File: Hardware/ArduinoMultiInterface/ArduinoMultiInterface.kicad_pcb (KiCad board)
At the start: 2 copper layers, 119.9 x 64.3 mm, 28 parts, among them J1 PORT1, J2 I2C, J3 SPI, J4 SER, SW1 SW_RESET, U1 ATmega328-P, U2 74HC165, U3 74HC595, U4 74HC574, U5 74HC574, U6 74HC574, U7 74HC04, U9 74LS20, Y1 20MHz

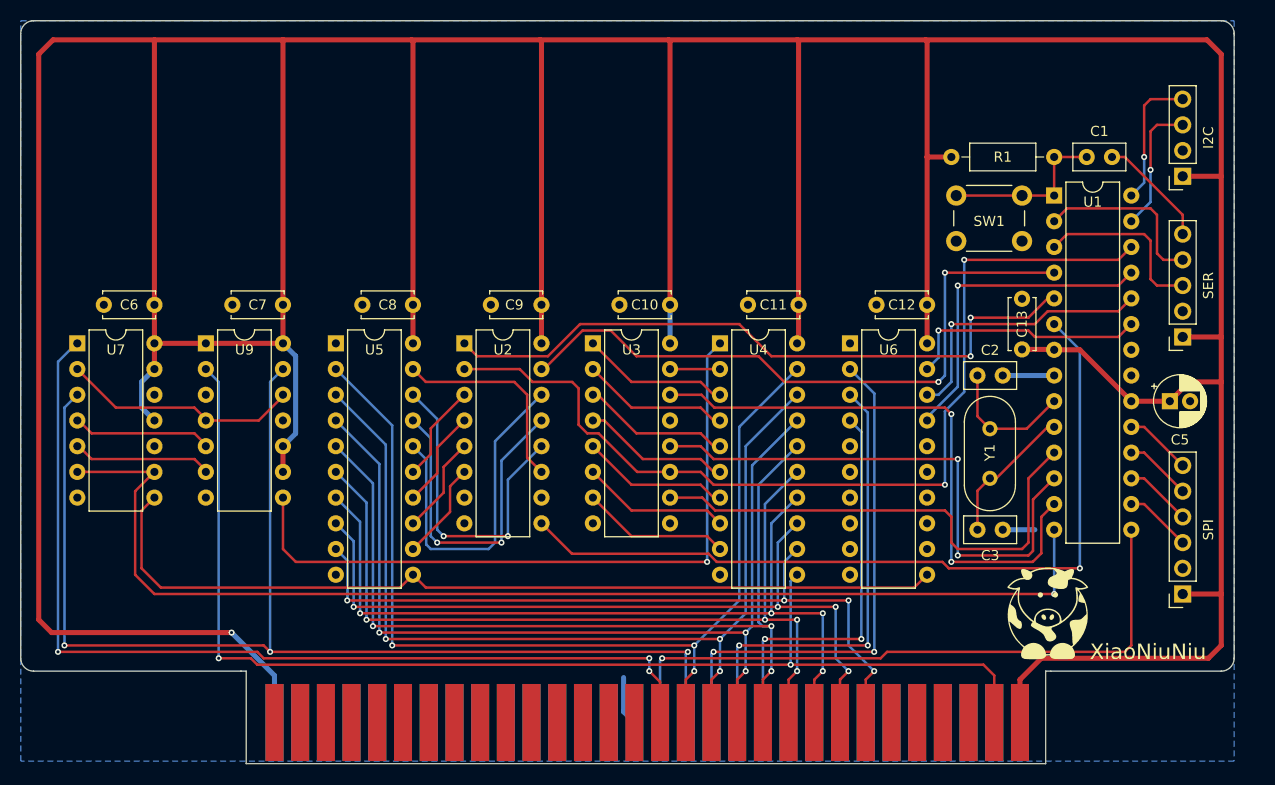
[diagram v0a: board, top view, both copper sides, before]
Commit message: Add nfr24l01 protocol
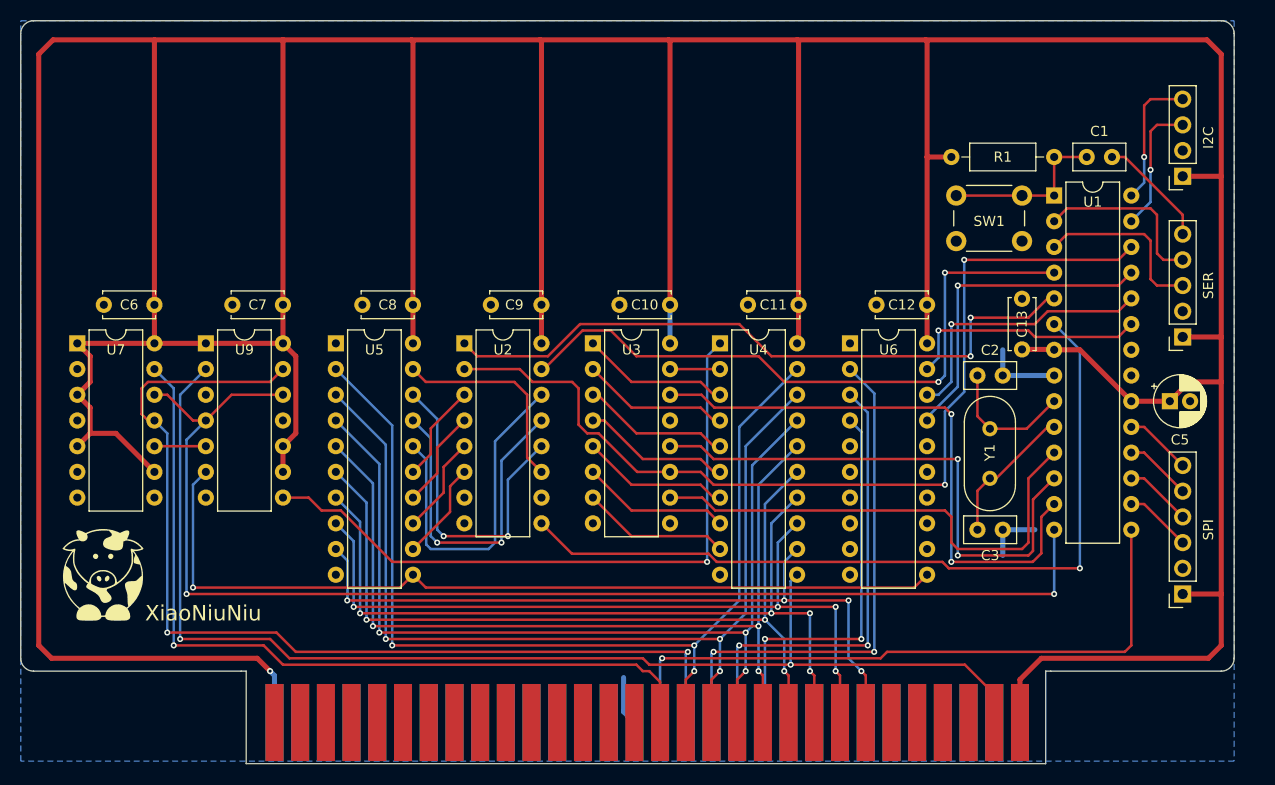
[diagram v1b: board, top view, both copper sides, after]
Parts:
- moved XiaoNiuNiu 93.4 mm to (97.8, 130.2)
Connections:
- U7 pad 1: /PORT1CSB -> +5V
- U7 pad 10: unconnected-(U7-Pad10) -> Net-(U7-Pad10)
- U7 pad 11: +5V -> /RW
- U7 pad 12: unconnected-(U7-Pad12) -> PCINT
- U7 pad 13: +5V -> /PORT1CSB
- U7 pad 2: Net-(U7-Pad2) -> unconnected-(U7-Pad2)
- U7 pad 3: /RW -> +5V
- U7 pad 4: Net-(U7-Pad4) -> unconnected-(U7-Pad4)
- U7 pad 5: Net-(U7-Pad5) -> +5V
- U7 pad 6: PCINT -> unconnected-(U7-Pad6)
- U7 pad 8: WE -> unconnected-(U7-Pad8)
- U7 pad 9: PCINT -> +5V
- U9 pad 12: Net-(U7-Pad2) -> PCINT
- U9 pad 4: Net-(U7-Pad2) -> PCINT
- U9 pad 5: Net-(U7-Pad4) -> Net-(U7-Pad10)
- U9 pad 6: Net-(U7-Pad5) -> WE
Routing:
- net /RW: track 122.7 -> 99.0 mm, vias 3 -> 2
- net Net-(U7-Pad2): track 23.6 -> 0.00 mm
- net +5V: track 569.8 -> 590.3 mm
- net /PORT1CSB: track 96.8 -> 81.7 mm, vias 3 -> 1
- net Net-(U7-Pad5): track 13.8 -> 0.00 mm
- net Net-(U7-Pad4): track 13.8 -> 0.00 mm
- net PCINT: track 116.5 -> 124.8 mm, vias 1 -> 2
- net Net-(U7-Pad10): track 0.00 -> 5.08 mm
- net GND: track 13.1 -> 18.2 mm
- net RE: track 69.6 -> 66.7 mm
- net /D4: track 84.8 -> 82.3 mm, vias 4 -> 3
- net /D3: track 88.9 -> 86.5 mm
- net /D5: track 81.8 -> 80.3 mm
- net WE: track 87.5 -> 86.1 mm, vias 0 -> 1
- net /D6: track 78.0 -> 77.3 mm
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
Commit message: Add ArduinoMultiInterface
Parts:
- Y1: footprint Crystal:Crystal_HC18-U_Vertical -> Crystal:Crystal_HC49-4H_Vertical
- moved XiaoNiuNiu 2.01 mm to (97.2, 132.1)
- moved J4 1.91 mm to (206.4, 106.7)
- moved J2 1.91 mm to (206.4, 90.8)
- moved J3 1.78 mm to (206.2, 132.1)
- moved C3 0.26 mm to (184.2, 126.0)
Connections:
- net /CLOCK renamed CLOCK
- net /IRQ3B renamed IRQ3B
- net /PORT1CSB renamed PORT1CSB
- net /RW renamed RW
- U7 pad 1: +5V -> WE
- U7 pad 12: PCINT -> Net-(U7-Pad12)
- U7 pad 2: unconnected-(U7-Pad2) -> Net-(U7-Pad2)
- U7 pad 3: +5V -> Net-(U7-Pad2)
- U7 pad 4: unconnected-(U7-Pad4) -> Net-(U7-Pad4)
- U7 pad 5: +5V -> Net-(U7-Pad4)
- U7 pad 6: unconnected-(U7-Pad6) -> Net-(U7-Pad6)
- U7 pad 8: unconnected-(U7-Pad8) -> PCINT
- U7 pad 9: +5V -> Net-(U7-Pad6)
- U9 pad 12: PCINT -> Net-(U7-Pad12)
- U9 pad 4: PCINT -> Net-(U7-Pad12)
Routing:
- net +5V: track 590.3 -> 569.5 mm
- net PCINT: track 124.8 -> 104.4 mm
- net Net-(U7-Pad12): track 0.00 -> 14.8 mm
- net WE: track 86.1 -> 97.8 mm, vias 1 -> 0
- net Net-(U7-Pad6): track 0.00 -> 7.62 mm
- net GND: track 18.2 -> 13.6 mm
- net IRQ3B: track 64.7 -> 61.0 mm
- net /D0: track 98.9 -> 102.6 mm, vias 3 -> 4
- net /D4: track 82.3 -> 85.9 mm, vias 3 -> 4
- net Net-(U2-D3): track 34.0 -> 37.5 mm, vias 0 -> 2
- net Net-(U2-D1): track 31.8 -> 35.0 mm
- net Net-(U2-D2): track 33.1 -> 36.2 mm
- net Net-(J4-Pin_5): track 11.3 -> 14.0 mm
- net Net-(U7-Pad4): track 0.00 -> 2.54 mm
- net Net-(U7-Pad2): track 0.00 -> 2.54 mm
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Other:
- rule pad_to_mask_clearance: 0 -> 0.08
- board text added: "Arduino Multi-Interface v1"
- board text added: "CS"
- board text added: "GND"
- board text added: "MISO"
- board text added: "MOSI"
- board text added: "RST"
- board text added: "RX"
- board text added: "SCK"
- board text added: "SCL"
- board text added: "SDA"
- board text added: "TX"
- board text added: "VCC"
